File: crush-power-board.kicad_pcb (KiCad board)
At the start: 4 copper layers, 101.6 x 120.6 mm, 109 parts, among them J1 XT90PW-F, J2 1x2 Header, J3 Molex Micro Fit 3.0, J4 Barrel_Jack, J5 2157601008, U1 BD9G341AEFJ, U2 SIC461ED-T1-GE3, U3 SIC461ED-T1-GE3, U4 BD9G341AEFJ

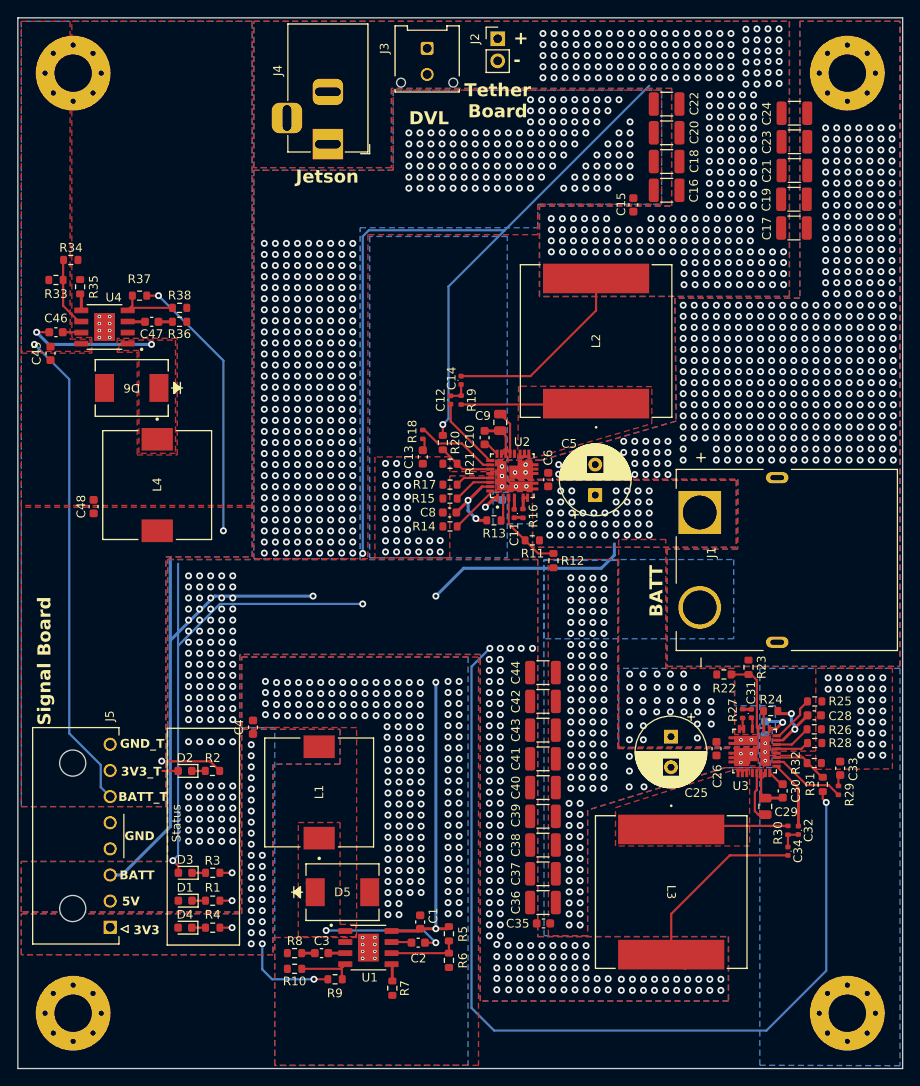
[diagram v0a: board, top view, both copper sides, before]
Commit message: use 6-32 mounting holes
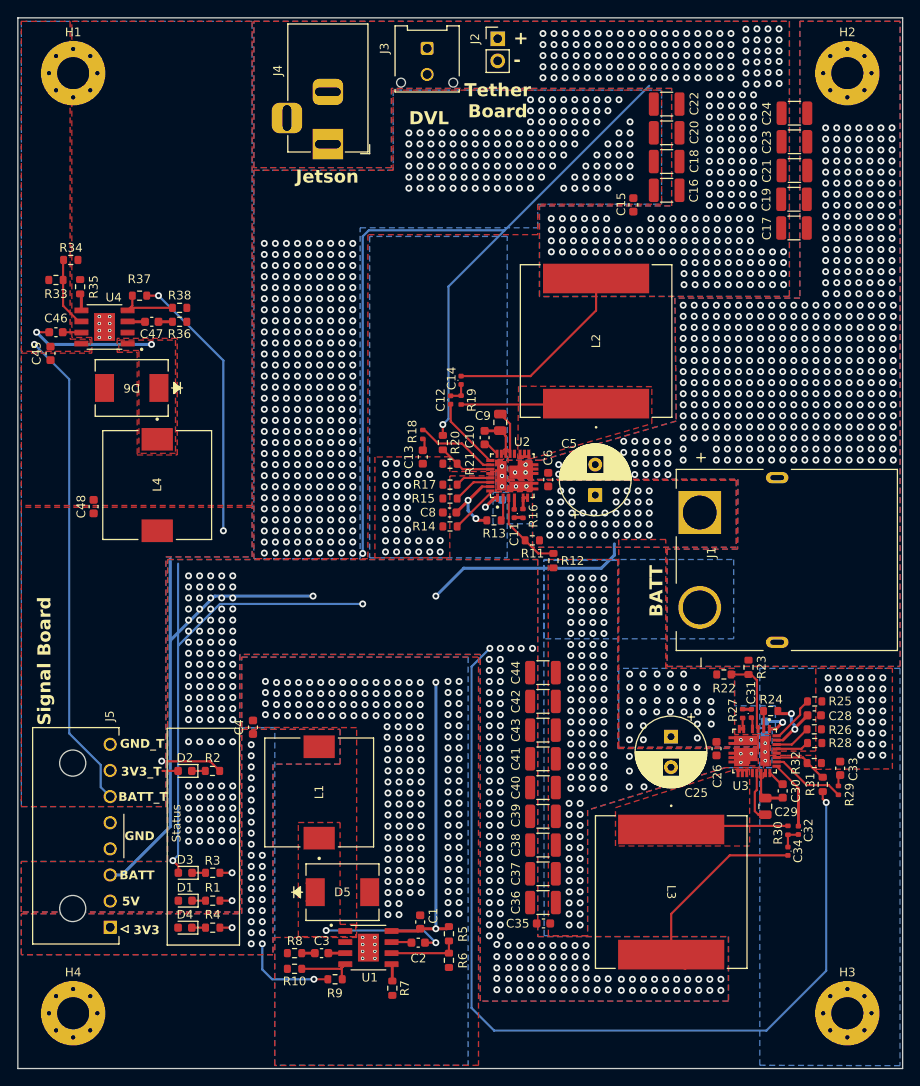
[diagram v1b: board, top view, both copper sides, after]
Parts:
- H1, H2, H3, H4: footprint MountingHole:MountingHole_4.3mm_M4_Pad_Via -> MountingHole:MountingHole_3.7mm_Pad_Via

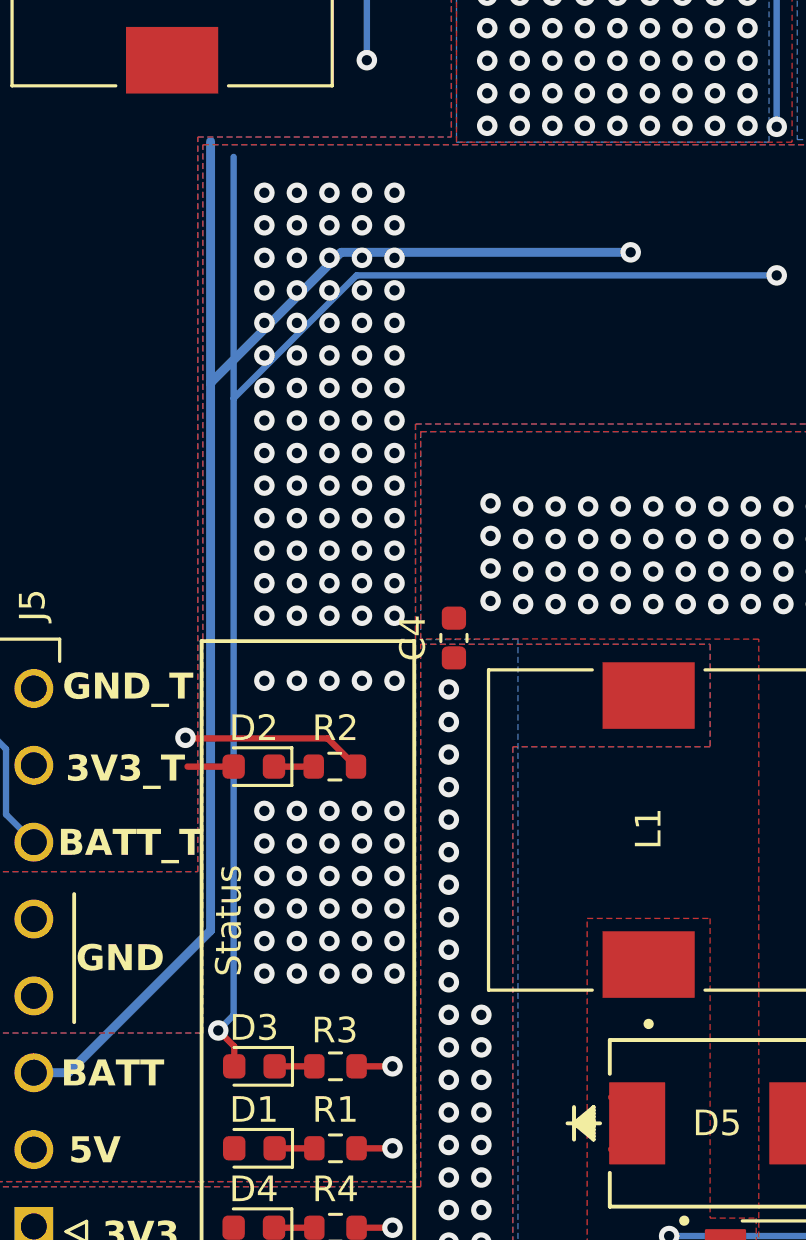
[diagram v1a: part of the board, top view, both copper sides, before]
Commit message: label 12v status indicator
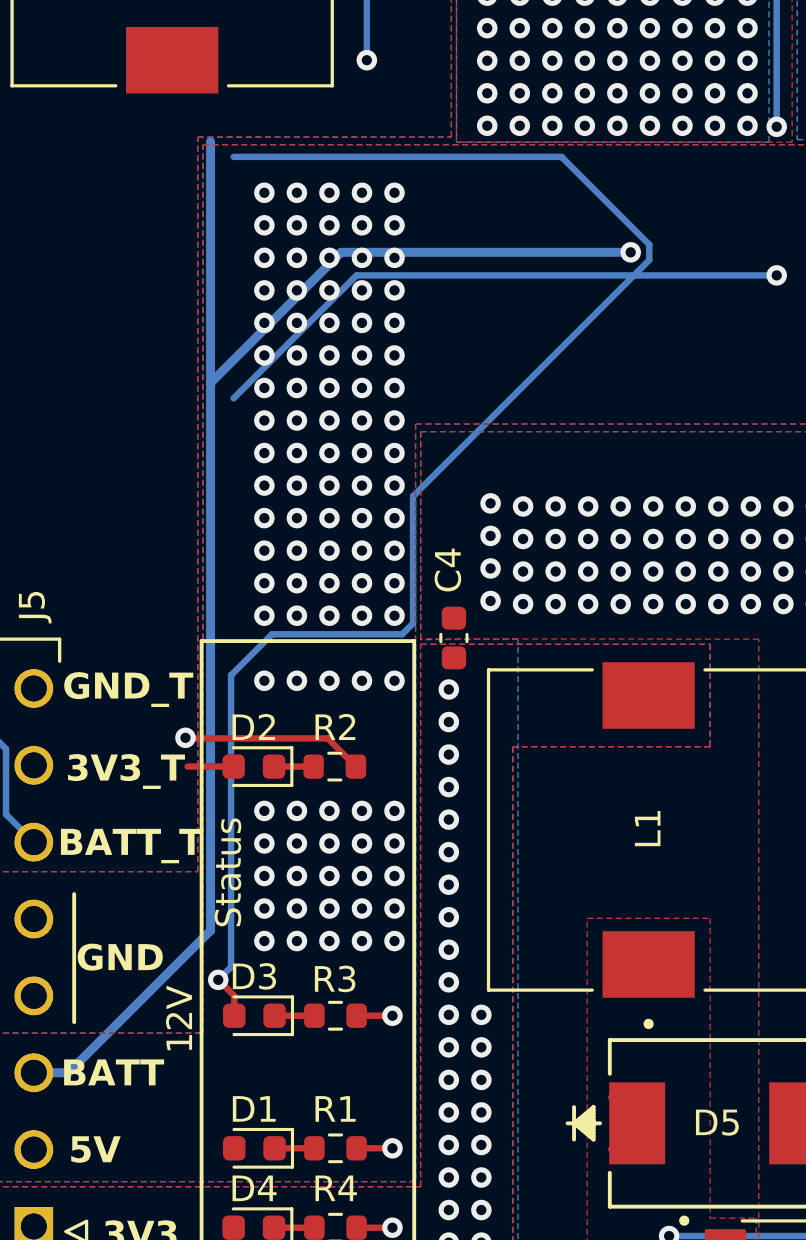
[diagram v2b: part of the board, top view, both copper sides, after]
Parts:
- moved D3 1.97 mm to (31.9, 108.9)
- moved R3 1.97 mm to (35.1, 108.9)
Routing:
- net 12V: track 190.5 -> 212.4 mm
- net 5V: vias 232 -> 227
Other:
- board text added: "12V"
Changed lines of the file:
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@@
     (property "ki_keywords" "cap capacitor")
     (attr smd)
-    (fp_text reference "C4" (at 0 -1.6 90) (layer "F.SilkS")
+    (fp_text reference "C4" (at 2.655 -0.2 90) (layer "F.SilkS")
         (effects (font (size 1 1) (thickness 0.15)))
     )
@@
   )
   (footprint "LED_SMD:LED_0603_1608Metric" (layer "F.Cu")
-    (at 31.9125 110.875 180)
+    (at 31.9125 108.9 180)
     (descr "LED SMD 0603 (1608 Metric), square (rectangular) end terminal, IPC_7351 nominal, (Body size source: http://www.tortai-tech.com/upload/download/2011102023233369053.pdf), generated with kicad-footprint-generator")
     (tags "LED")
@@
   )
   (footprint "Resistor_SMD:R_0603_1608Metric" (layer "F.Cu")
-    (at 35.075 110.875)
+    (at 35.075 108.9)
     (descr "Resistor SMD 0603 (1608 Metric), square (rectangular) end terminal, IPC_7351 nominal, (Body size source: IPC-SM-782 page 72, https://www.pcb-3d.com/wordpress/wp-content/uploads/ipc-sm-782a_amendment_1_and_2.pdf), generated with kicad-footprint-generator")
     (tags "resistor")
@@
     (effects (font (size 1.016 1.016) (thickness 0.150012) bold))
   )
+  (gr_text "12V" (at 29.6 110.4 90) (layer "F.SilkS")
+    (effects (font (size 1 1) (thickness 0.15)) (justify left bottom))
+  )
   (gr_text "DVL" (at 57.6 25.1) (layer "F.SilkS")
     (effects (font (size 1.5 1.5) (thickness 0.3) bold) (justify left bottom))
@@
     (effects (font (size 1.5 1.5) (thickness 0.3) bold) (justify left bottom))
   )
-  (gr_text "Status" (at 31.5 107.375 90) (layer "F.SilkS")
+  (gr_text "Status" (at 31.5 105.5 90) (layer "F.SilkS")
     (effects (font (size 1 1) (thickness 0.15)) (justify left bottom))
   )
@@
   (segment (start 100.4766 102.2983) (end 100.5266 102.2483) (width 0.35) (layer "F.Cu") (net 2))
   (segment (start 68.725 60.725) (end 68.1 60.1) (width 0.25) (layer "F.Cu") (net 2))
-  (segment (start 35.9 110.875) (end 37.3 110.875) (width 0.25) (layer "F.Cu") (net 2))
+  (segment (start 35.9 108.9) (end 37.3 108.9) (width 0.25) (layer "F.Cu") (net 2))
   (segment (start 66.3 60.125) (end 68.075 60.125) (width 0.35) (layer "F.Cu") (net 2))
   (segment (start 98.05 101.8217) (end 98.5266 102.2983) (width 0.25) (layer "F.Cu") (net 2))
@@
   (via (at 44.81 52.57) (size 0.8) (drill 0.4) (layers "F.Cu" "B.Cu") (free) (net 2))
   (via (at 63.37 114.3) (size 0.8) (drill 0.4) (layers "F.Cu" "B.Cu") (free) (net 2))
-  (via (at 37.3 110.875) (size 0.8) (drill 0.4) (layers "F.Cu" "B.Cu") (free) (net 2))
+  (via (at 37.3 108.9) (size 0.8) (drill 0.4) (layers "F.Cu" "B.Cu") (free) (net 2))
   (via (at 63.37 99.06) (size 0.8) (drill 0.4) (layers "F.Cu" "B.Cu") (free) (net 2))
   (via (at 71.57 23.37) (size 0.8) (drill 0.4) (layers "F.Cu" "B.Cu") (free) (net 2))
@@
   (segment (start 71.56 53.84) (end 63.6 53.84) (width 0.25) (layer "F.Cu") (net 16))
   (segment (start 79.1 46.3) (end 71.56 53.84) (width 0.25) (layer "F.Cu") (net 16))
-  (segment (start 31.125 110.875) (end 31.125 110.1) (width 0.25) (layer "F.Cu") (net 16))
-  (segment (start 31.125 110.1) (end 30.5 109.475) (width 0.25) (layer "F.Cu") (net 16))
+  (segment (start 31.125 108.9) (end 31.125 108.125) (width 0.25) (layer "F.Cu") (net 16))
+  (segment (start 31.125 108.125) (end 30.5 107.5) (width 0.25) (layer "F.Cu") (net 16))
   (segment (start 61.5 60.65) (end 61.5 59.4) (width 0.25) (layer "F.Cu") (net 16))
   (via (at 75.54 19.58) (size 0.8) (drill 0.4) (layers "F.Cu" "B.Cu") (free) (net 16))
@@
   (via (at 77.77 39.57) (size 0.8) (drill 0.4) (layers "F.Cu" "B.Cu") (free) (net 16))
   (via (at 91.74 40.8) (size 0.8) (drill 0.4) (layers "F.Cu" "B.Cu") (free) (net 16))
-  (via (at 30.5 109.475) (size 0.8) (drill 0.4) (layers "F.Cu" "B.Cu") (net 16))
+  (via (at 30.5 107.5) (size 0.8) (drill 0.4) (layers "F.Cu" "B.Cu") (net 16))
   (via (at 93.01 39.57) (size 0.8) (drill 0.4) (layers "F.Cu" "B.Cu") (free) (net 16))
   (via (at 89.2 42.07) (size 0.8) (drill 0.4) (layers "F.Cu" "B.Cu") (free) (net 16))
@@
   (via (at 97.1804 31.6992) (size 0.8) (drill 0.4) (layers "F.Cu" "B.Cu") (free) (net 16))
   (segment (start 52.3 80) (end 52.3 74.2) (width 0.25) (layer "In1.Cu") (net 16))
-  (segment (start 31.1 108.875) (end 31.1 75.375) (width 0.25) (layer "B.Cu") (net 16))
+  (segment (start 47.325 79.400305) (end 47.325 78.799695) (width 0.25) (layer "B.Cu") (net 16))
+  (segment (start 38.105 88.620305) (end 47.325 79.400305) (width 0.25) (layer "B.Cu") (net 16))
+  (segment (start 32.600305 94.01) (end 37.680305 94.01) (width 0.25) (layer "B.Cu") (net 16))
+  (segment (start 30.5 107.5) (end 31 107) (width 0.25) (layer "B.Cu") (net 16))
   (segment (start 35.9 80) (end 52.3 80) (width 0.25) (layer "B.Cu") (net 16))
   (segment (start 62.15 58.75) (end 61.5 59.4) (width 0.25) (layer "B.Cu") (net 16))
+  (segment (start 37.680305 94.01) (end 38.105 93.585305) (width 0.25) (layer "B.Cu") (net 16))
   (segment (start 52.3 37.8) (end 53 37.1) (width 0.25) (layer "B.Cu") (net 16))
   (segment (start 31.1 84.8) (end 35.9 80) (width 0.25) (layer "B.Cu") (net 16))
   (segment (start 62.15 43.55) (end 62.15 58.75) (width 0.25) (layer "B.Cu") (net 16))
-  (segment (start 30.5 109.475) (end 31.1 108.875) (width 0.25) (layer "B.Cu") (net 16))
+  (segment (start 31 107) (end 31 95.610305) (width 0.25) (layer "B.Cu") (net 16))
+  (segment (start 38.105 93.585305) (end 38.105 88.620305) (width 0.25) (layer "B.Cu") (net 16))
   (segment (start 53 37.1) (end 68.6 37.1) (width 0.25) (layer "B.Cu") (net 16))
   (segment (start 52.3 74.2) (end 52.3 74.4) (width 0.25) (layer "B.Cu") (net 16))
+  (segment (start 31 95.610305) (end 32.600305 94.01) (width 0.25) (layer "B.Cu") (net 16))
   (segment (start 68.6 37.1) (end 62.15 43.55) (width 0.25) (layer "B.Cu") (net 16))
   (segment (start 52.3 74.2) (end 52.3 37.8) (width 0.25) (layer "B.Cu") (net 16))
+  (segment (start 47.325 78.799695) (end 43.900305 75.375) (width 0.25) (layer "B.Cu") (net 16))
   (segment (start 68.6 37.1) (end 85.2 20.5) (width 0.25) (layer "B.Cu") (net 16))
+  (segment (start 43.900305 75.375) (end 31.1 75.375) (width 0.25) (layer "B.Cu") (net 16))
   (segment (start 101.9266 94.3944) (end 101.7956 94.3944) (width 0.25) (layer "F.Cu") (net 17))
   (segment (start 103.3956 92.7944) (end 101.9266 94.2634) (width 0.35) (layer "F.Cu") (net 17))
@@
   (via (at 84.54 124.37) (size 0.8) (drill 0.4) (layers "F.Cu" "B.Cu") (free) (net 25))
   (via (at 85.81 123.1) (size 0.8) (drill 0.4) (layers "F.Cu" "B.Cu") (free) (net 25))
-  (via (at 33.57 107.255) (size 0.8) (drill 0.4) (layers "F.Cu" "B.Cu") (free) (net 25))
   (via (at 68.1 97.8) (size 0.8) (drill 0.4) (layers "F.Cu" "B.Cu") (free) (net 25))
   (via (at 32.3 104.715) (size 0.8) (drill 0.4) (layers "F.Cu" "B.Cu") (free) (net 25))
@@
   (via (at 66.83 93.99) (size 0.8) (drill 0.4) (layers "F.Cu" "B.Cu") (free) (net 25))
   (via (at 37.38 79.315) (size 0.8) (drill 0.4) (layers "F.Cu" "B.Cu") (free) (net 25))
-  (via (at 34.84 107.255) (size 0.8) (drill 0.4) (layers "F.Cu" "B.Cu") (free) (net 25))
   (via (at 32.3 90.745) (size 0.8) (drill 0.4) (layers "F.Cu" "B.Cu") (free) (net 25))
   (via (at 34.84 95.825) (size 0.8) (drill 0.4) (layers "F.Cu" "B.Cu") (free) (net 25))
@@
   (via (at 68.1 85.1) (size 0.8) (drill 0.4) (layers "F.Cu" "B.Cu") (free) (net 25))
   (via (at 74.14 121.77) (size 0.8) (drill 0.4) (layers "F.Cu" "B.Cu") (free) (net 25))
-  (via (at 32.3 107.255) (size 0.8) (drill 0.4) (layers "F.Cu" "B.Cu") (free) (net 25))
   (via (at 66.83 115.58) (size 0.8) (drill 0.4) (layers "F.Cu" "B.Cu") (free) (net 25))
   (via (at 69.06 123.04) (size 0.8) (drill 0.4) (layers "F.Cu" "B.Cu") (free) (net 25))
@@
   (via (at 76.68 124.31) (size 0.8) (drill 0.4) (layers "F.Cu" "B.Cu") (free) (net 25))
   (via (at 71.6 121.77) (size 0.8) (drill 0.4) (layers "F.Cu" "B.Cu") (free) (net 25))
-  (via (at 37.38 107.255) (size 0.8) (drill 0.4) (layers "F.Cu" "B.Cu") (free) (net 25))
   (via (at 37.38 78.045) (size 0.8) (drill 0.4) (layers "F.Cu" "B.Cu") (free) (net 25))
   (via (at 36.11 88.205) (size 0.8) (drill 0.4) (layers "F.Cu" "B.Cu") (free) (net 25))
@@
   (via (at 68.1 92.72) (size 0.8) (drill 0.4) (layers "F.Cu" "B.Cu") (free) (net 25))
   (via (at 72.87 119.23) (size 0.8) (drill 0.4) (layers "F.Cu" "B.Cu") (free) (net 25))
-  (via (at 36.11 107.255) (size 0.8) (drill 0.4) (layers "F.Cu" "B.Cu") (free) (net 25))
   (via (at 69.06 120.5) (size 0.8) (drill 0.4) (layers "F.Cu" "B.Cu") (free) (net 25))
   (via (at 33.57 89.475) (size 0.8) (drill 0.4) (layers "F.Cu" "B.Cu") (free) (net 25))
@@
   (segment (start 32.7 114.075) (end 34.25 114.075) (width 0.25) (layer "F.Cu") (net 31))
   (segment (start 34.225 99.175) (end 32.675 99.175) (width 0.25) (layer "F.Cu") (net 32))
-  (segment (start 34.35 110.875) (end 32.7 110.875) (width 0.25) (layer "F.Cu") (net 33))
+  (segment (start 34.35 108.9) (end 32.7 108.9) (width 0.25) (layer "F.Cu") (net 33))
   (segment (start 34.25 117.175) (end 32.675 117.175) (width 0.25) (layer "F.Cu") (net 34))
   (segment (start 78.4 57) (end 77.9 57.5) (width 0.25) (layer "F.Cu") (net 35))
